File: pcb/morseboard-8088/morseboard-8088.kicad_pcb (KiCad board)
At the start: 2 copper layers, 127 x 127 mm, 61 parts, among them J1 USB_B, J2 UART1, SW1 SW_SPDT, SW2 INTPORT, SW4 NMI, SW6 RESET, U1 8088, U10 74HCT273, U11 TL16C550, U12 74HC245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

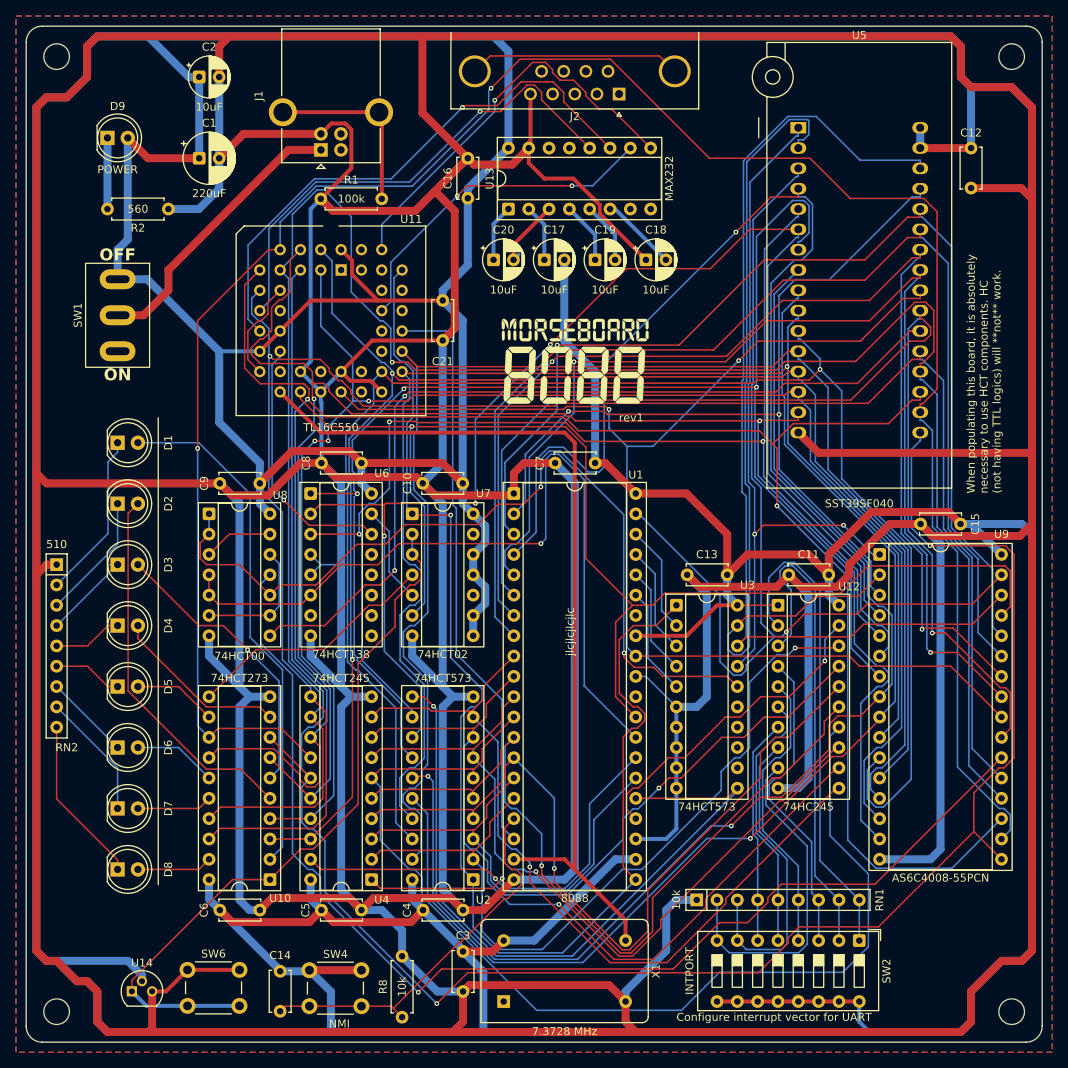
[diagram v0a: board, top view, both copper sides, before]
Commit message: Fixing erroneous board layout
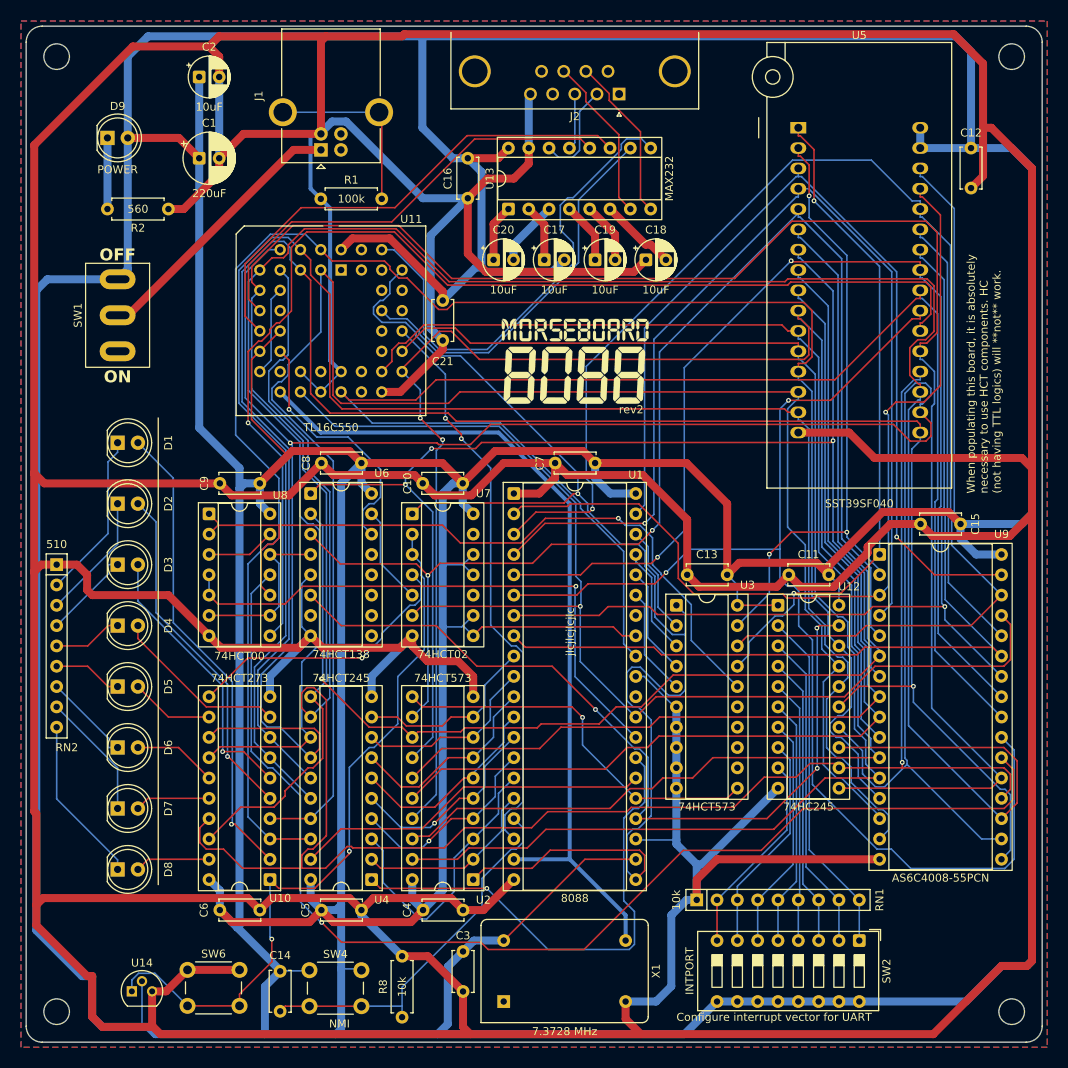
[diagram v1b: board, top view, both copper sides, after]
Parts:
- moved C16 5.00 mm to (80.6, 43.2), turned to -90 degrees
- renumbered G*** to G001
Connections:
- U1 pad 28: ~{M} -> IO/~{M}
- U12 pad 11: AD7 -> D7
- U12 pad 12: AD6 -> D6
- U12 pad 13: AD5 -> D5
- U12 pad 14: AD4 -> D4
- U12 pad 15: AD3 -> D3
- U12 pad 16: AD2 -> D2
- U12 pad 17: AD1 -> D1
- U12 pad 18: AD0 -> D0
- U13 pad 13: R1IN -> UART3
- U13 pad 14: T1OUT -> UART2
- U13 pad 7: T2OUT -> UART8
- U13 pad 8: R2IN -> UART7
- U6 pad 4: GND -> ~{IO}/M
- U6 pad 6: ~{M} -> ~{INTA}
- U8 pad 12: M -> ~{IO}/M
- U8 pad 4: ~{M} -> IO/~{M}
- U8 pad 5: ~{M} -> IO/~{M}
- U8 pad 6: M -> ~{IO}/M
- U8 pad 9: M -> ~{IO}/M
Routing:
- net GND: track 1400.2 -> 1166.9 mm
- net VCC: track 1023.8 -> 1142.8 mm
- net AD4: track 135.6 -> 25.4 mm
- net ~{M}: track 99.7 -> 0.00 mm, vias 1 -> 0
- net AD6: track 101.6 -> 23.3 mm, vias 1 -> 0
- net AD0: track 100.0 -> 23.3 mm, vias 1 -> 0
- net AD7: track 99.1 -> 23.3 mm, vias 1 -> 0
- net AD3: track 100.2 -> 25.4 mm
- net AD2: track 98.2 -> 25.4 mm
- net IO/~{M}: track 0.00 -> 71.9 mm, vias 0 -> 1
- net AD5: track 95.9 -> 25.4 mm, vias 1 -> 0
- net ~{INTA}: track 40.3 -> 104.6 mm, vias 1 -> 3
- net AD1: track 86.7 -> 35.5 mm, vias 1 -> 0
- net D7: track 231.6 -> 275.5 mm, vias 1 -> 0
- net ALE: track 89.9 -> 48.5 mm
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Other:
- board text added: "rev2"
- board text removed: "rev1"

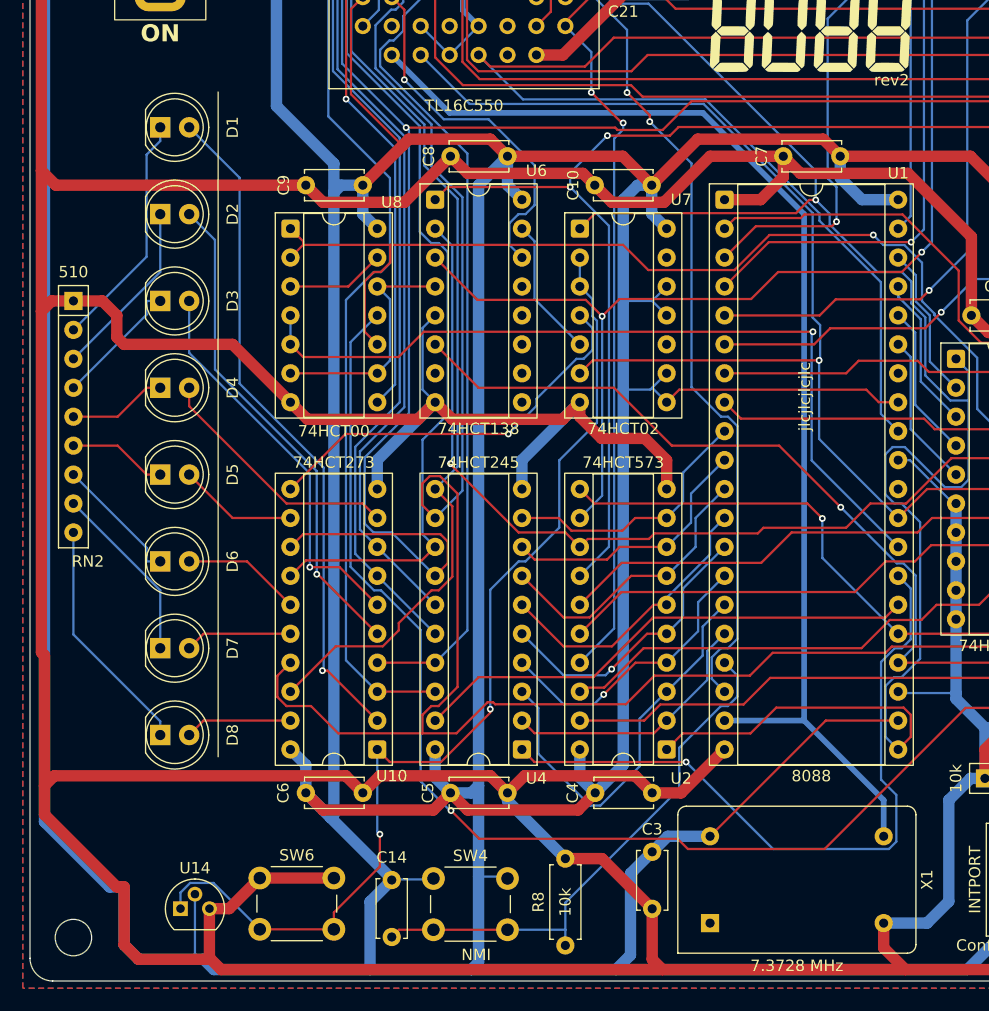
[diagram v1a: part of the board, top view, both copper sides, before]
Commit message: Further building menu and fixing minor mistakes in PCB
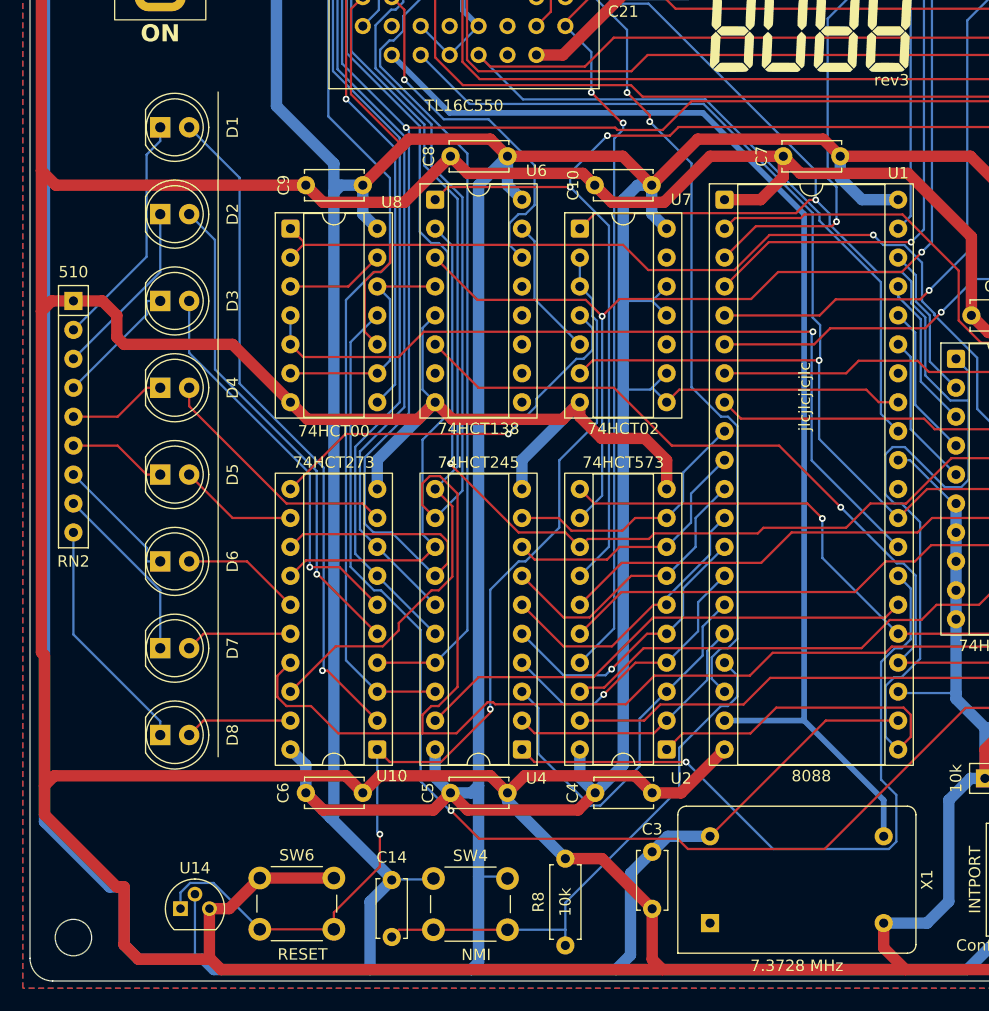
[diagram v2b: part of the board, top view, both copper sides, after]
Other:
- board text added: "rev3"
- board text removed: "rev2"
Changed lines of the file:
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@@
 		(property "Value" "RESET"
 			(at 3.75 6.7 0)
-			(layer "F.Fab")
+			(layer "F.SilkS")
 			(effects
 				(font
@@
 		(tags "R")
 		(property "Reference" "RN2"
-			(at 22.86 -1.27 0)
+			(at 22.86 0 0)
 			(layer "F.SilkS")
 			(effects
@@
 		)
 	)
-	(gr_text "rev2"
+	(gr_text "rev3"
 		(at 99.484423 75.184 0)
 		(layer "F.SilkS")
